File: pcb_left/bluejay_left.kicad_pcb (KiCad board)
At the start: 2 copper layers, 147 x 140.5 mm, 81 parts, among them J1 SJ-43514, U1 ATmega328P-PU, Y1 16MHz

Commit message: Ground a couple mounting holes so as to ground plate and base too
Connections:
- H2 pad 1: (no net) -> GND
- H3 pad 1: (no net) -> GND
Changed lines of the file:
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@@
     (property "Sheetfile" "bluejay_left.kicad_sch")
     (property "Sheetname" "")
-    (property "exclude_from_bom" "")
-    (attr exclude_from_pos_files exclude_from_bom)
+    (attr exclude_from_pos_files)
     (fp_text reference "H2" (at 0 -3.2) (layer "F.SilkS")
       (effects (font (size 1 1) (thickness 0.15)))
@@
     (fp_circle (center 0 0) (end 2.2 0) (layer "Cmts.User") (width 0.15) (fill none))
     (fp_circle (center 0 0) (end 2.45 0) (layer "F.CrtYd") (width 0.05) (fill none))
-    (pad "1" thru_hole circle (at 0 0) (size 4.4 4.4) (drill 2.2) (layers *.Cu *.Mask))
+    (pad "1" thru_hole circle (at 0 0) (size 4.4 4.4) (drill 2.2) (layers *.Cu *.Mask)
+      (net 1 "GND") (pinfunction "1") (pintype "input"))
   )
   (footprint "BlueJay footprints:D_DO-35_SOD27_P5.08mm_Horizontal" (layer "F.Cu")
@@
     (property "Sheetfile" "bluejay_left.kicad_sch")
     (property "Sheetname" "")
-    (property "exclude_from_bom" "")
-    (attr exclude_from_pos_files exclude_from_bom)
+    (attr exclude_from_pos_files)
     (fp_text reference "H3" (at 0 -3.2) (layer "F.SilkS")
       (effects (font (size 1 1) (thickness 0.15)))
@@
     (fp_circle (center 0 0) (end 2.2 0) (layer "Cmts.User") (width 0.15) (fill none))
     (fp_circle (center 0 0) (end 2.45 0) (layer "F.CrtYd") (width 0.05) (fill none))
-    (pad "1" thru_hole circle (at 0 0) (size 4.4 4.4) (drill 2.2) (layers *.Cu *.Mask))
+    (pad "1" thru_hole circle (at 0 0) (size 4.4 4.4) (drill 2.2) (layers *.Cu *.Mask)
+      (net 1 "GND") (pinfunction "1") (pintype "input"))
   )
   (footprint "BlueJay footprints:D_DO-35_SOD27_P5.08mm_Horizontal" (layer "F.Cu")

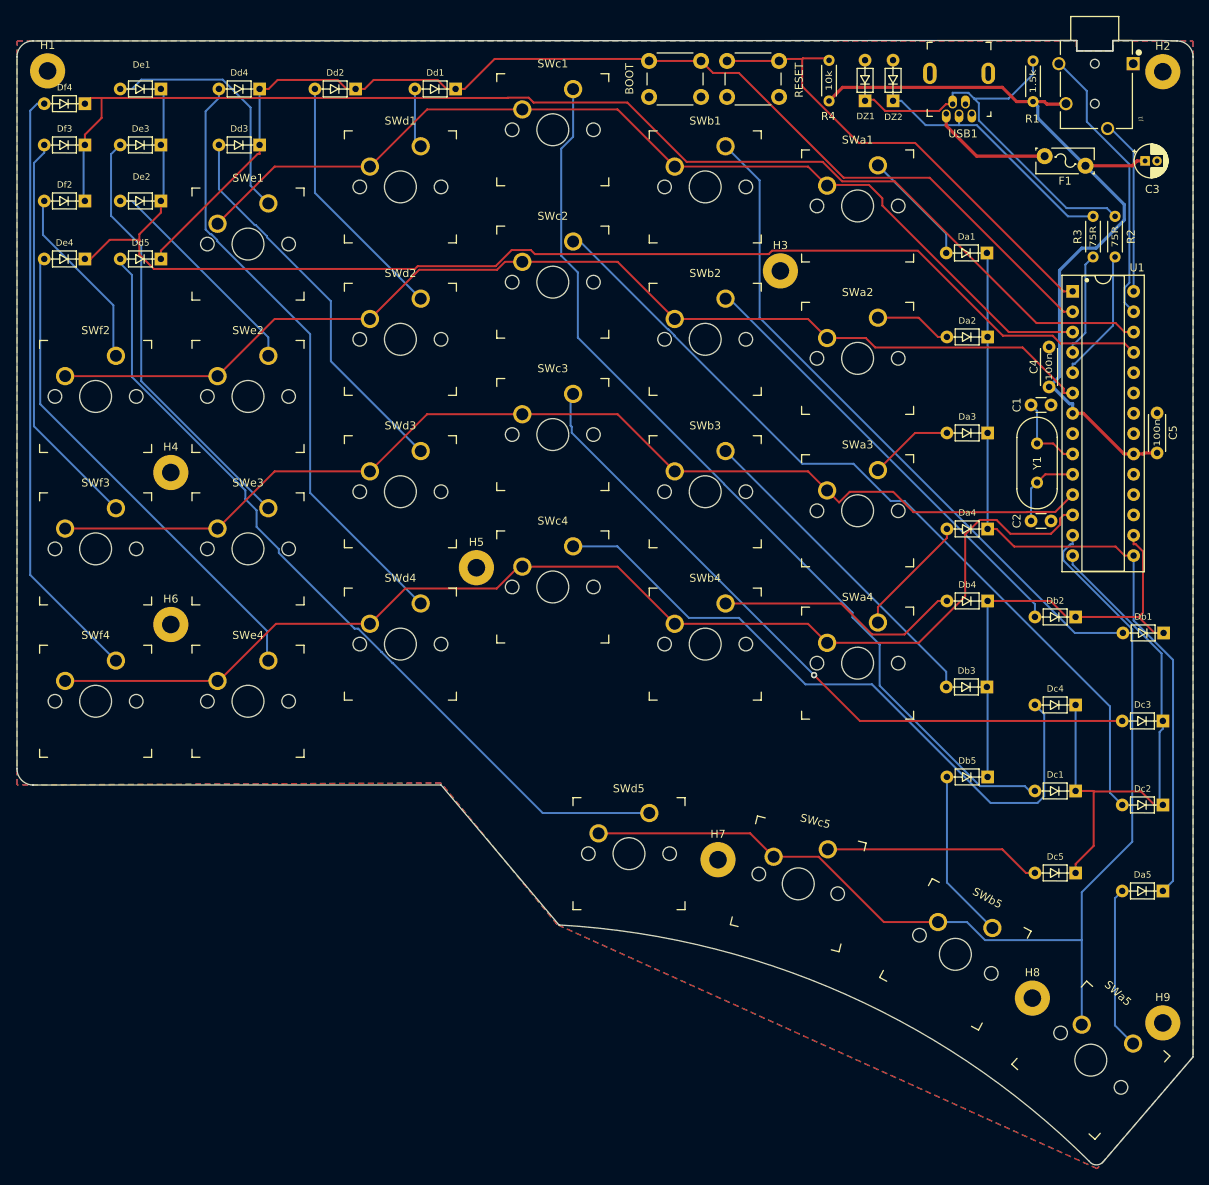
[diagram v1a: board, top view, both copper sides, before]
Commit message: Create base pcb
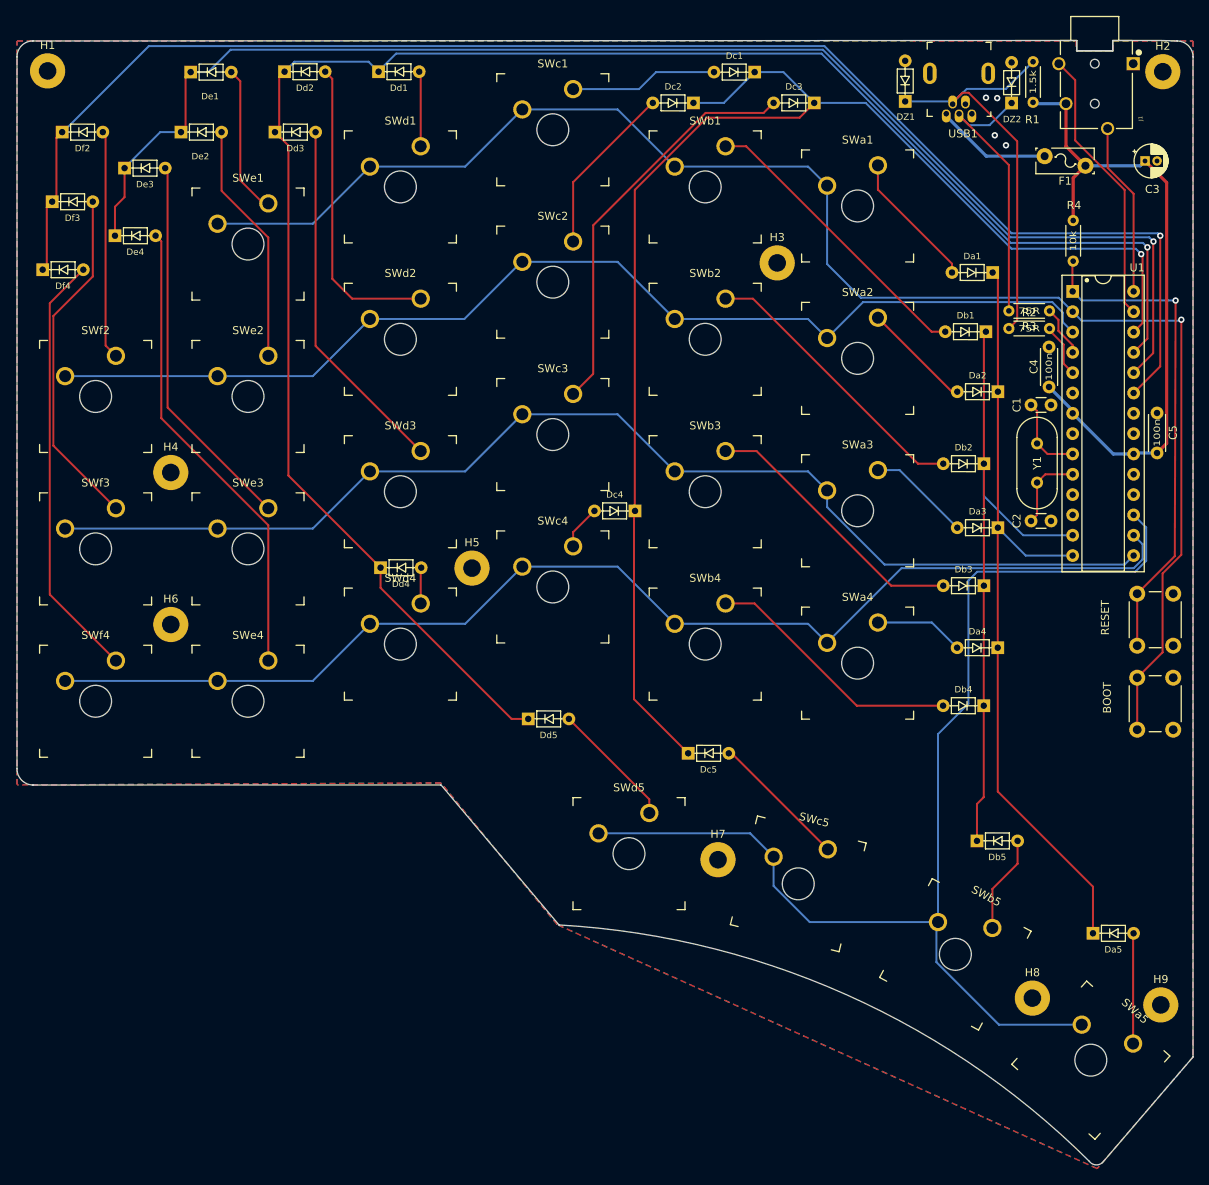
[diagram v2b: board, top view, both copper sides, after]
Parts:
- SWa1, SWa2, SWa3, SWa4, SWa5, SWb1, SWb2, SWb3, SWb4, SWb5, SWc1, SWc2, SWc3, SWc4, SWc5, SWd1, SWd2, SWd3, SWd4, SWd5, SWe1, SWe2, SWe3, SWe4, SWf2, SWf3, SWf4: footprint BlueJay footprints:SW_MX -> BlueJay footprints:SW_MX_Plate
- moved Dc2 105.6 mm to (-0.20, -48.6)
- moved PB2 103.5 mm to (54.0, 29.8), turned to 90 degrees
- moved Dc1 98.4 mm to (7.45, -52.5)
- moved PB1 89.3 mm to (54.0, 19.2), turned to 90 degrees
- moved Dc3 88.7 mm to (14.9, -48.6)
- moved Dd5 72.0 mm to (-23.4, 28.4), turned to 0 degrees
- moved Dd4 61.2 mm to (-41.9, 9.50), turned to 0 degrees
- moved Dc4 60.2 mm to (-7.50, 2.40)
- moved Dc5 53.1 mm to (-3.40, 32.7), turned to 0 degrees
- moved Db1 43.7 mm to (36.4, -20.0)
- moved R4 34.0 mm to (46.0, -33.9), turned to -90 degrees
- moved Db2 22.3 mm to (36.1, -3.50)
- moved Df4 22.2 mm to (-84.1, -27.8), turned to 0 degrees
- moved Da4 14.9 mm to (37.8, 19.5)
- moved DZ2 14.8 mm to (38.3, -47.3)
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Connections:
- net Net-(DZ1-Pad1) renamed /USBPRE_D-
- net Net-(DZ2-Pad1) renamed /USBPRE_D+
- PB2 pad 1: /colD -> /row1
- U1 pad 11: /row3 -> unconnected-(U1-Pad11)
- U1 pad 12: /row4 -> unconnected-(U1-Pad12)
- U1 pad 13: /row5 -> /colB
- U1 pad 14: /colC -> /colA
- U1 pad 15: /colA -> /row3
- U1 pad 16: /colB -> /row4
- U1 pad 17: unconnected-(U1-Pad17) -> /row5
- U1 pad 2: /colD -> /row1
- U1 pad 23: unconnected-(U1-Pad23) -> /colF
- U1 pad 24: unconnected-(U1-Pad24) -> /colE
- U1 pad 25: /colE -> /colD
- U1 pad 26: /colF -> /colC
- U1 pad 3: /row1 -> /row2
- U1 pad 6: /row2 -> unconnected-(U1-Pad6)
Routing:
- net /colC: track 69.7 -> 177.5 mm, vias 0 -> 1
- net Net-(Dc1-Pad2): track 116.5 -> 18.5 mm
- net Net-(Dd5-Pad2): track 104.7 -> 15.9 mm
- net /colD: track 144.6 -> 229.5 mm, vias 0 -> 1
- net Net-(Dc2-Pad2): track 104.2 -> 21.5 mm
- net Net-(Dc4-Pad2): track 84.4 -> 5.53 mm
- net Net-(Dd4-Pad2): track 76.2 -> 4.49 mm
- net /row1: track 124.9 -> 196.7 mm, vias 0 -> 1
- net Net-(Db1-Pad2): track 84.9 -> 37.1 mm
- net Net-(Dc3-Pad2): track 88.7 -> 51.0 mm, vias 1 -> 0
- net /colF: track 157.4 -> 190.8 mm, vias 0 -> 1
- net /colB: track 56.8 -> 81.3 mm
- net Net-(Df4-Pad2): track 75.3 -> 54.0 mm
- net Net-(Db2-Pad2): track 56.1 -> 35.8 mm
- net VCC: track 101.9 -> 83.5 mm
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
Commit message: add logo
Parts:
- added G***: LOGO, BlueJay footprints:bluejay_logo_small, F.Cu at (49.5, 37.2)

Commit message: work on plate
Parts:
- moved R2 15.6 mm to (43.0, -36.0)
- moved R3 15.5 mm to (43.0, -38.1)
- moved R1 2.85 mm to (41.6, -51.0)
- moved DZ2 2.64 mm to (38.6, -44.7)
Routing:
- net /USBPRE_D-: track 53.5 -> 35.4 mm
- net /USBPRE_D+: track 35.6 -> 19.4 mm
- net /USB_D-: track 6.72 -> 22.3 mm
- net /USB_D+: track 6.38 -> 21.9 mm
- net VCC: track 83.5 -> 84.4 mm
- net GND: vias 4 -> 0
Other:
- board text added: "JLCJLCJLCJLC"
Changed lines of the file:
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@@
   )
   (footprint "BlueJay footprints:D_DO-35_SOD27_P5.08mm_Horizontal" (layer "F.Cu")
-    (at 38.3 -47.3125 90)
+    (at 38.58 -44.69 90)
     (descr "Diode, DO-35_SOD27 series, Axial, Horizontal, pin pitch=7.62mm, , length*diameter=4*2mm^2, , http://www.diodes.com/_files/packages/DO-35.pdf")
     (tags "Diode DO-35_SOD27 series Axial Horizontal pin pitch 7.62mm  length 4mm diameter 2mm")
@@
   )
   (footprint "BlueJay footprints:R_Axial_DIN0204_L3.6mm_D1.6mm_P5.08mm_Horizontal" (layer "F.Cu")
-    (at 40.9812 -53.75 -90)
+    (at 41.64 -50.98 -90)
     (descr "Resistor, Axial_DIN0204 series, Axial, Horizontal, pin pitch=5.08mm, 0.167W, length*diameter=3.6*1.6mm^2, http://cdn-reichelt.de/documents/datenblatt/B400/1_4W%23YAG.pdf")
     (tags "Resistor Axial_DIN0204 series Axial Horizontal pin pitch 5.08mm 0.167W length 3.6mm diameter 1.6mm")
@@
   )
   (footprint "BlueJay footprints:R_Axial_DIN0204_L3.6mm_D1.6mm_P5.08mm_Horizontal" (layer "F.Cu")
-    (at 43.04 -22.6 180)
+    (at 42.99 -38.08 180)
     (descr "Resistor, Axial_DIN0204 series, Axial, Horizontal, pin pitch=5.08mm, 0.167W, length*diameter=3.6*1.6mm^2, http://cdn-reichelt.de/documents/datenblatt/B400/1_4W%23YAG.pdf")
     (tags "Resistor Axial_DIN0204 series Axial Horizontal pin pitch 5.08mm 0.167W length 3.6mm diameter 1.6mm")
@@
   )
   (footprint "BlueJay footprints:R_Axial_DIN0204_L3.6mm_D1.6mm_P5.08mm_Horizontal" (layer "F.Cu")
-    (at 43.04 -20.4 180)
+    (at 42.99 -35.95 180)
     (descr "Resistor, Axial_DIN0204 series, Axial, Horizontal, pin pitch=5.08mm, 0.167W, length*diameter=3.6*1.6mm^2, http://cdn-reichelt.de/documents/datenblatt/B400/1_4W%23YAG.pdf")
     (tags "Resistor Axial_DIN0204 series Axial Horizontal pin pitch 5.08mm 0.167W length 3.6mm diameter 1.6mm")
@@
   (gr_line (start 39.85 -56.4) (end -84.024489 -56.3437) (layer "Edge.Cuts") (width 0.1))
   (gr_arc (start 49.7812 83.7263) (mid 48.888799 84.147698) (end 48.0112 83.6963) (layer "Edge.Cuts") (width 0.1))
-  (via (at 36.5 -49.2) (size 0.8) (drill 0.4) (layers "F.Cu" "B.Cu") (free) (net 1))
-  (via (at 37.6 -43.3) (size 0.8) (drill 0.4) (layers "F.Cu" "B.Cu") (free) (net 1))
-  (via (at 35.1 -49.25) (size 0.8) (drill 0.4) (layers "F.Cu" "B.Cu") (free) (net 1))
-  (via (at 36.2 -44.55) (size 0.8) (drill 0.4) (layers "F.Cu" "B.Cu") (free) (net 1))
+  (gr_text "JLCJLCJLCJLC" (at -80.15 35.09) (layer "B.Cu")
+    (effects (font (size 1 1) (thickness 0.2)) (justify mirror))
+  )
   (segment (start 42.7874 -4.7175) (end 45.9312 -4.7175) (width 0.25) (layer "F.Cu") (net 2))
   (segment (start 41.4812 -10.0937) (end 40.7312 -10.8437) (width 0.25) (layer "F.Cu") (net 2))
@@
   (segment (start 53.6774 -4.8437) (end 53.5512 -4.7175) (width 0.4) (layer "B.Cu") (net 4))
   (segment (start 47.5312 -40.7437) (end 54.3812 -40.7437) (width 0.4) (layer "B.Cu") (net 4))
-  (segment (start 41.1512 -48.5) (end 40.9812 -48.67) (width 0.4) (layer "B.Cu") (net 4))
+  (segment (start 43.23 -48.5) (end 41.64 -46.91) (width 0.4) (layer "B.Cu") (net 4))
   (segment (start 51.0112 -4.7175) (end 45.9312 -9.7975) (width 0.4) (layer "B.Cu") (net 4))
   (segment (start 45.9312 -10.1437) (end 42.9812 -13.0937) (width 0.4) (layer "B.Cu") (net 4))
-  (segment (start 45.1 -48.5) (end 41.1512 -48.5) (width 0.4) (layer "B.Cu") (net 4))
+  (segment (start 45.1 -48.5) (end 43.23 -48.5) (width 0.4) (layer "B.Cu") (net 4))
   (segment (start 45.9312 -9.7975) (end 45.9312 -10.1437) (width 0.4) (layer "B.Cu") (net 4))
+  (segment (start 41.64 -46.91) (end 41.64 -45.9) (width 0.4) (layer "B.Cu") (net 4))
   (segment (start 53.5512 -4.7175) (end 51.0112 -4.7175) (width 0.4) (layer "B.Cu") (net 4))
   (segment (start 36.5863 -26.7437) (end 35.93 -27.4) (width 0.25) (layer "F.Cu") (net 5))
@@
   (segment (start -73.66 21.1138) (end -81.927021 12.846779) (width 0.25) (layer "F.Cu") (net 37))
   (segment (start -81.927021 -23.560479) (end -77.7375 -27.75) (width 0.25) (layer "F.Cu") (net 37))
-  (segment (start 30.9312 -48.630458) (end 32.168962 -49.86822) (width 0.25) (layer "F.Cu") (net 38))
-  (segment (start 39 -43.8) (end 39 -21.44) (width 0.25) (layer "F.Cu") (net 38))
-  (segment (start 30.9312 -48.4437) (end 30.9312 -48.630458) (width 0.25) (layer "F.Cu") (net 38))
-  (segment (start 32.93178 -49.86822) (end 39 -43.8) (width 0.25) (layer "F.Cu") (net 38))
-  (segment (start 39 -21.44) (end 37.96 -20.4) (width 0.25) (layer "F.Cu") (net 38))
-  (segment (start 32.168962 -49.86822) (end 32.93178 -49.86822) (width 0.25) (layer "F.Cu") (net 38))
-  (segment (start 30.9312 -48.630458) (end 32.168962 -49.86822) (width 0.25) (layer "B.Cu") (net 38))
+  (segment (start 29.25668 -44.60332) (end 29.25668 -47.94668) (width 0.25) (layer "F.Cu") (net 38))
+  (segment (start 29.25668 -47.94668) (end 29.7537 -48.4437) (width 0.25) (layer "F.Cu") (net 38))
+  (segment (start 29.7537 -48.4437) (end 30.9312 -48.4437) (width 0.25) (layer "F.Cu") (net 38))
+  (segment (start 37.91 -35.95) (end 29.25668 -44.60332) (width 0.25) (layer "F.Cu") (net 38))
   (segment (start 30.9312 -48.4437) (end 30.9312 -48.630458) (width 0.25) (layer "B.Cu") (net 38))
   (segment (start 30.5924 -48.7825) (end 30.9312 -48.4437) (width 0.25) (layer "B.Cu") (net 38))
-  (segment (start 32.7 -50.35) (end 37.5812 -50.35) (width 0.25) (layer "B.Cu") (net 38))
-  (segment (start 32.168962 -49.86822) (end 32.21822 -49.86822) (width 0.25) (layer "B.Cu") (net 38))
-  (segment (start 32.21822 -49.86822) (end 32.7 -50.35) (width 0.25) (layer "B.Cu") (net 38))
+  (segment (start 40.99 -50.98) (end 41.64 -50.98) (width 0.25) (layer "B.Cu") (net 38))
+  (segment (start 39.925489 -49.915489) (end 40.99 -50.98) (width 0.25) (layer "B.Cu") (net 38))
+  (segment (start 30.9312 -48.630458) (end 32.216231 -49.915489) (width 0.25) (layer "B.Cu") (net 38))
   (segment (start 25 -48.7825) (end 30.5924 -48.7825) (width 0.25) (layer "B.Cu") (net 38))
-  (segment (start 37.5812 -50.35) (end 40.9812 -53.75) (width 0.25) (layer "B.Cu") (net 38))
-  (segment (start 37.96 -40.84) (end 37.96 -22.6) (width 0.25) (layer "F.Cu") (net 39))
-  (segment (start 32.98082 -45.81918) (end 37.96 -40.84) (width 0.25) (layer "F.Cu") (net 39))
+  (segment (start 32.216231 -49.915489) (end 39.925489 -49.915489) (width 0.25) (layer "B.Cu") (net 38))
   (segment (start 31.7312 -47.2437) (end 31.7312 -47.056942) (width 0.25) (layer "F.Cu") (net 39))
+  (segment (start 32.98082 -45.81918) (end 37.96 -40.84) (width 0.25) (layer "F.Cu") (net 39))
   (segment (start 31.7312 -47.056942) (end 32.968962 -45.81918) (width 0.25) (layer "F.Cu") (net 39))
+  (segment (start 37.96 -40.84) (end 37.96 -38.13) (width 0.25) (layer "F.Cu") (net 39))
+  (segment (start 37.96 -38.13) (end 37.91 -38.08) (width 0.25) (layer "F.Cu") (net 39))
   (segment (start 32.968962 -45.81918) (end 32.98082 -45.81918) (width 0.25) (layer "F.Cu") (net 39))
-  (segment (start 35.53668 -45.81918) (end 38.3 -48.5825) (width 0.25) (layer "B.Cu") (net 39))
+  (segment (start 35.6775 -45.96) (end 38.58 -45.96) (width 0.25) (layer "B.Cu") (net 39))
   (segment (start 31.7312 -47.2437) (end 31.7312 -47.056942) (width 0.25) (layer "B.Cu") (net 39))
   (segment (start 31.7312 -47.056942) (end 32.968962 -45.81918) (width 0.25) (layer "B.Cu") (net 39))
+  (segment (start 35.53668 -45.81918) (end 35.6775 -45.96) (width 0.25) (layer "B.Cu") (net 39))
   (segment (start 32.968962 -45.81918) (end 35.53668 -45.81918) (width 0.25) (layer "B.Cu") (net 39))
   (segment (start 30.1312 -47.2437) (end 30.1312 -46.950876) (width 0.4) (layer "B.Cu") (net 40))
@@
   (segment (start 58.8 -23.9) (end 57.812989 -23.912989) (width 0.25) (layer "B.Cu") (net 43))
   (segment (start 44.806689 -16.002011) (end 45.9312 -14.8775) (width 0.25) (layer "F.Cu") (net 44))
-  (segment (start 43.04 -20.4) (end 43.04 -20.16) (width 0.25) (layer "F.Cu") (net 44))
-  (segment (start 43.04 -20.16) (end 44.806689 -18.393311) (width 0.25) (layer "F.Cu") (net 44))
+  (segment (start 42.99 -35.95) (end 42.99 -20.21) (width 0.25) (layer "F.Cu") (net 44))
   (segment (start 44.806689 -18.393311) (end 44.806689 -16.002011) (width 0.25) (layer "F.Cu") (net 44))
+  (segment (start 42.99 -20.21) (end 44.806689 -18.393311) (width 0.25) (layer "F.Cu") (net 44))
   (segment (start 45.9312 -18.3188) (end 45.9312 -17.4175) (width 0.25) (layer "F.Cu") (net 45))
+  (segment (start 42.99 -38.08) (end 44.151762 -36.918238) (width 0.25) (layer "F.Cu") (net 45))
   (segment (start 44.151762 -20.098238) (end 45.9312 -18.3188) (width 0.25) (layer "F.Cu") (net 45))
-  (segment (start 43.04 -22.6) (end 44.151762 -21.488238) (width 0.25) (layer "F.Cu") (net 45))
-  (segment (start 44.151762 -21.488238) (end 44.151762 -20.098238) (width 0.25) (layer "F.Cu") (net 45))
+  (segment (start 44.151762 -36.918238) (end 44.151762 -20.098238) (width 0.25) (layer "F.Cu") (net 45))
   (segment (start 59.516988 7.883012) (end 59.516988 -21.498695) (width 0.25) (layer "F.Cu") (net 46))
   (segment (start 57.175489 20.074511) (end 57.175489 10.224511) (width 0.25) (layer "F.Cu") (net 46))

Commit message: Fine tune pcbs
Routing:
- net GND: vias 0 -> 2
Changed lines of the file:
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@@
   (gr_line (start 39.85 -56.4) (end -84.024489 -56.3437) (layer "Edge.Cuts") (width 0.1))
   (gr_arc (start 49.7812 83.7263) (mid 48.888799 84.147698) (end 48.0112 83.6963) (layer "Edge.Cuts") (width 0.1))
-  (gr_text "JLCJLCJLCJLC" (at -80.15 35.09) (layer "B.Cu")
+  (gr_text "JLCJLCJLCJLC" (at -80.15 35.09) (layer "B.SilkS")
     (effects (font (size 1 1) (thickness 0.2)) (justify mirror))
   )
+  (via (at 36 -40) (size 0.8) (drill 0.4) (layers "F.Cu" "B.Cu") (free) (net 1))
+  (via (at 49.75 -22.75) (size 0.8) (drill 0.4) (layers "F.Cu" "B.Cu") (free) (net 1))
   (segment (start 42.7874 -4.7175) (end 45.9312 -4.7175) (width 0.25) (layer "F.Cu") (net 2))
   (segment (start 41.4812 -10.0937) (end 40.7312 -10.8437) (width 0.25) (layer "F.Cu") (net 2))
@@
     (connect_pads (clearance 0.508))
     (min_thickness 0.254) (filled_areas_thickness no)
-    (fill yes (thermal_gap 0.508) (thermal_bridge_width 0.508) (island_removal_mode 1) (island_area_min 0))
+    (fill yes (thermal_gap 0.508) (thermal_bridge_width 0.508))
     (polygon
       (pts
